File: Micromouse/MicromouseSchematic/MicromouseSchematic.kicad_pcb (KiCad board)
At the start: 2 copper layers, 0 parts

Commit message: Schematics clear, moved all footprints to pcb and voltage regulator completed. The layout begins
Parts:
- added C1: 0.47 μF, Capacitor_SMD:C_0201_0603Metric, F.Cu at (62.0, 97.2)
- added C11: 100nF, Capacitor_SMD:C_0402_1005Metric, F.Cu at (108.4, 161.7)
- added C19: 0.1u, Capacitor_SMD:C_0402_1005Metric, F.Cu at (251.6, 118.7)
- added C2: 22 µF, Capacitor_SMD:C_0402_1005Metric, F.Cu at (71.5, 38.0)
- added C20: 10p, Capacitor_SMD:C_0402_1005Metric, F.Cu at (251.6, 120.6)
- added C21: 10p, Capacitor_SMD:C_0402_1005Metric, F.Cu at (251.6, 122.6)
- added C22: 2.2u, Capacitor_SMD:C_0402_1005Metric, F.Cu at (251.6, 124.6)
- added C23: 2.2u, Capacitor_SMD:C_0402_1005Metric, F.Cu at (251.6, 126.5)
- added C24: 100n, Capacitor_SMD:C_0402_1005Metric, F.Cu at (251.6, 128.5)
- added C25: 100n, Capacitor_SMD:C_0402_1005Metric, F.Cu at (254.5, 118.7)
- added C26: 100n, Capacitor_SMD:C_0402_1005Metric, F.Cu at (254.5, 120.6)
- added C27: 100n, Capacitor_SMD:C_0402_1005Metric, F.Cu at (254.5, 122.6)
- added C28: 6.8p, Capacitor_SMD:C_0402_1005Metric, F.Cu at (254.5, 124.6)
- added C29: 100n, Capacitor_SMD:C_0402_1005Metric, F.Cu at (254.5, 126.5)
- added C3: 0.47 μF, Capacitor_SMD:C_0402_1005Metric, F.Cu at (59.3, 91.5)
- added C30: 100n, Capacitor_SMD:C_0402_1005Metric, F.Cu at (254.5, 128.5)
- added C31: 6.8p, Capacitor_SMD:C_0402_1005Metric, F.Cu at (257.4, 118.7)
- added C32: 10u, Capacitor_SMD:C_0402_1005Metric, F.Cu at (257.4, 120.6)
- added C33: 1u, Capacitor_SMD:C_0402_1005Metric, F.Cu at (257.4, 122.6)
- added C34: 10n, Capacitor_SMD:C_0402_1005Metric, F.Cu at (257.4, 124.6)
- added C35: 1u, Capacitor_SMD:C_0402_1005Metric, F.Cu at (257.4, 126.5)
- added C36: 0.47 μF, Capacitor_SMD:C_0402_1005Metric, F.Cu at (59.3, 93.4)
- added C37: 0.47 μF, Capacitor_SMD:C_0402_1005Metric, F.Cu at (59.3, 95.4)
- added C38: 0.1 μF, Capacitor_SMD:C_0402_1005Metric, F.Cu at (194.1, 37.0)
- added C39: 2.2 μF, Capacitor_SMD:C_0402_1005Metric, F.Cu at (194.1, 39.0)
- added C4: 220 nF, Capacitor_SMD:C_0402_1005Metric, F.Cu at (194.1, 29.2)
- added C40: 10 nF, Capacitor_SMD:C_0402_1005Metric, F.Cu at (194.1, 41.0)
- added C41: 1uF, Capacitor_SMD:C_0402_1005Metric, F.Cu at (129.5, 57.3)
- added C42: 1uF, Capacitor_SMD:C_0402_1005Metric, F.Cu at (129.5, 59.3)
- added C43: 1uF, Capacitor_SMD:C_0402_1005Metric, F.Cu at (129.5, 61.3)
- added C44: 1uF, Capacitor_SMD:C_0402_1005Metric, F.Cu at (129.5, 63.3)
- added C5: 100 nF, Capacitor_SMD:C_0402_1005Metric, F.Cu at (194.1, 31.1)
- added C6: 100 nF, Capacitor_SMD:C_0402_1005Metric, F.Cu at (194.1, 33.1)
- added C7: 10 μF, Capacitor_SMD:C_0402_1005Metric, F.Cu at (194.1, 35.1)
- added C9: 4.7uF, Capacitor_SMD:C_0402_1005Metric, F.Cu at (108.4, 159.7)
- added Cin_MD1: 22 μF, Capacitor_SMD:C_0402_1005Metric, F.Cu at (59.3, 97.4)
- added Cin_VR1: 10 µF, Capacitor_SMD:C_0402_1005Metric, F.Cu at (57.5, 38.0)
- added D1: SFH4550, LED_THT:LED_D5.0mm_IRGrey, F.Cu at (117.0, 31.0)
- added D2: SFH4550, LED_THT:LED_D5.0mm_IRGrey, F.Cu at (117.0, 38.4)
- added D3: SFH4550, LED_THT:LED_D5.0mm_IRGrey, F.Cu at (124.5, 31.0)
- added D4: SFH4550, LED_THT:LED_D5.0mm_IRGrey, F.Cu at (124.5, 38.4)
- added FB1: FerriteBead, Resistor_SMD:R_0805_2012Metric, F.Cu at (254.0, 141.5)
- added J1: Conn_01x06_MountingPin, Connector_JST:JST_PH_B6B-PH-K_1x06_P2.00mm_Vertical, F.Cu at (56.3, 80.1)
- added J10: Conn_01x06_MountingPin, Connector_JST:JST_ZH_B6B-ZR_1x06_P1.50mm_Vertical, F.Cu at (219.2, 156.6)
- added J2: Conn_01x06_MountingPin, Connector_JST:JST_PH_B6B-PH-K_1x06_P2.00mm_Vertical, F.Cu at (56.3, 86.7)
- added J3: Conn_01x03_Pin, Connector_JST:JST_PH_B3B-PH-K_1x03_P2.00mm_Vertical, F.Cu at (73.5, 41.5)
- added J4: Conn_01x02_Pin, Connector_JST:JST_PH_B2B-PH-K_1x02_P2.00mm_Vertical, F.Cu at (77.5, 35.5)
- added J5: Conn_01x06_MountingPin, Connector_JST:JST_ZH_B6B-ZR_1x06_P1.50mm_Vertical, F.Cu at (219.2, 151.1)
- added J6: IR_1, Connector_JST:JST_ZH_B4B-ZR_1x04_P1.50mm_Vertical, F.Cu at (117.0, 44.5)
- added J7: IR_2, Connector_JST:JST_ZH_B4B-ZR_1x04_P1.50mm_Vertical, F.Cu at (116.9, 50.1)
- added J8: IR_3, Connector_JST:JST_ZH_B4B-ZR_1x04_P1.50mm_Vertical, F.Cu at (117.0, 55.6)
- added J9: IR_4, Connector_JST:JST_ZH_B4B-ZR_1x04_P1.50mm_Vertical, F.Cu at (117.0, 61.1)
- added Q1: SFH300, LED_THT:LED_D5.0mm_Clear, F.Cu at (131.9, 31.0)
- added Q2: DMN3065LW-7, MM_DMN3065LW-7:DMN3065LW-7, F.Cu at (131.0, 43.9)
- added Q3: DMN3065LW-7, MM_DMN3065LW-7:DMN3065LW-7, F.Cu at (131.0, 47.5)
- added Q4: DMN3065LW-7, MM_DMN3065LW-7:DMN3065LW-7, F.Cu at (130.9, 51.2)
- added Q5: DMN3065LW-7, MM_DMN3065LW-7:DMN3065LW-7, F.Cu at (131.0, 54.6)
- added Q6: SFH300, LED_THT:LED_D5.0mm_Clear, F.Cu at (131.9, 38.4)
- added Q7: SFH300, LED_THT:LED_D5.0mm_Clear, F.Cu at (139.4, 31.0)
- added Q8: SFH300, LED_THT:LED_D5.0mm_Clear, F.Cu at (139.4, 38.4)
- added R1: 10k, Resistor_SMD:R_0603_1608Metric, F.Cu at (104.9, 153.1)
- added R2: 10k, Resistor_SMD:R_0603_1608Metric, F.Cu at (104.9, 155.6)
- added R20: 10k, Resistor_SMD:R_0603_1608Metric, F.Cu at (253.8, 144.3)
- added R21: 5 kΩ, Resistor_SMD:R_0805_2012Metric, F.Cu at (63.0, 92.0)
- added R22: 5 kΩ, Resistor_SMD:R_0805_2012Metric, F.Cu at (63.0, 94.9)
- added R23: 10 kΩ, Resistor_SMD:R_0603_1608Metric, F.Cu at (197.5, 29.4)
- added R24: 10 kΩ, Resistor_SMD:R_0603_1608Metric, F.Cu at (197.5, 31.9)
- added R25: 10k, Resistor_SMD:R_0603_1608Metric, F.Cu at (126.1, 43.4)
- added R26: 10 kΩ, Resistor_SMD:R_0603_1608Metric, F.Cu at (197.5, 34.5)
- added R27: 10 kΩ, Resistor_SMD:R_0603_1608Metric, F.Cu at (197.5, 37.0)
- added R28: 100, Resistor_SMD:R_0603_1608Metric, F.Cu at (126.1, 45.9)
- added R29: 10k, Resistor_SMD:R_0603_1608Metric, F.Cu at (126.1, 48.4)
- added R3: 10k, Resistor_SMD:R_0603_1608Metric, F.Cu at (104.9, 158.1)
- added R30: 100, Resistor_SMD:R_0603_1608Metric, F.Cu at (126.1, 50.9)
- added R31: 10k, Resistor_SMD:R_0603_1608Metric, F.Cu at (126.1, 53.5)
- added R32: 100, Resistor_SMD:R_0603_1608Metric, F.Cu at (126.1, 56.0)
- added R33: 10k, Resistor_SMD:R_0603_1608Metric, F.Cu at (126.1, 58.5)
- added R34: 100, Resistor_SMD:R_0603_1608Metric, F.Cu at (126.1, 61.0)
- added R35: 10 kΩ, Resistor_SMD:R_0603_1608Metric, F.Cu at (51.3, 78.6)
- added R36: 10 kΩ, Resistor_SMD:R_0603_1608Metric, F.Cu at (51.3, 81.1)
- added R37: 10 kΩ, Resistor_SMD:R_0603_1608Metric, F.Cu at (51.3, 83.7)
- added R38: 10 kΩ, Resistor_SMD:R_0603_1608Metric, F.Cu at (51.3, 86.2)
- added R39: 10 kΩ, Resistor_SMD:R_0603_1608Metric, F.Cu at (51.3, 88.7)
- added R4: 10k, Resistor_SMD:R_0603_1608Metric, F.Cu at (104.9, 160.6)
- added R40: 10 kΩ, Resistor_SMD:R_0603_1608Metric, F.Cu at (51.3, 91.2)
- added R41: 10 kΩ, Resistor_SMD:R_0603_1608Metric, F.Cu at (51.3, 93.7)
- added R42: 10 kΩ, Resistor_SMD:R_0603_1608Metric, F.Cu at (51.3, 96.2)
- added Renb1: 30kΩ, Resistor_SMD:R_0603_1608Metric, F.Cu at (60.7, 36.2)
- added Rent1: 62kΩ, Resistor_SMD:R_0603_1608Metric, F.Cu at (60.7, 39.6)
- added SW1: SW_Push, Button_Switch_THT:SW_SPST_Omron_B3F-40xx, F.Cu at (218.7, 122.9)
- added SW2: SW_Push, Button_Switch_THT:SW_SPST_Omron_B3F-40xx, F.Cu at (218.7, 138.5)
- added U1: VL53L1CXV0FY1, MM_VL53L4CDV0DH-1:LGA12_STM, F.Cu at (109.2, 155.3)
- added U11: MP6550GG-Z, MM_MP6550G-Z:MP6550_MNP, F.Cu at (55.5, 97.0)
- added U3: ICM-42688-P, MM_ICM_42688_P:ICM_42688_P, F.Cu at (202.2, 30.2)
- added U4: LIS2MDLTR, MM_LIS2MDLTR:LIS2MDLTR, F.Cu at (201.7, 34.1)
- added U5: STM32F746VETx, Package_QFP:LQFP-100_14x14mm_P0.5mm, F.Cu at (242.5, 146.0)
- added U7: MP6550GG-Z, MM_MP6550G-Z:MP6550_MNP, F.Cu at (55.5, 92.7)
- added VR1: TPSM861253RDXR, MM_TPSM861253RDXR:TPSM861253RDXR, F.Cu at (67.5, 38.3)
- added Y1: 8MHz, Crystal:Crystal_SMD_5032-2Pin_5.0x3.2mm, F.Cu at (253.9, 132.1)
- added Y2: 32.768kHz, Crystal:Crystal_SMD_3215-2Pin_3.2x1.5mm, F.Cu at (254.3, 138.4)
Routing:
- net GND: track 0.00 -> 44.0 mm
- net +7.4V: track 0.00 -> 31.5 mm
- net +3.3V: track 0.00 -> 16.8 mm
- net Net-(VR1-EN): track 0.00 -> 6.92 mm
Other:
- board outline added: 30.7 x 18.7 mm
- board text added: "Base board"
- board text added: "IMU&Mag"
- board text added: "IR Sensors"
- board text added: "Motor Drivers"
- board text added: "ToF"
- board text added: "Voltage regulator"

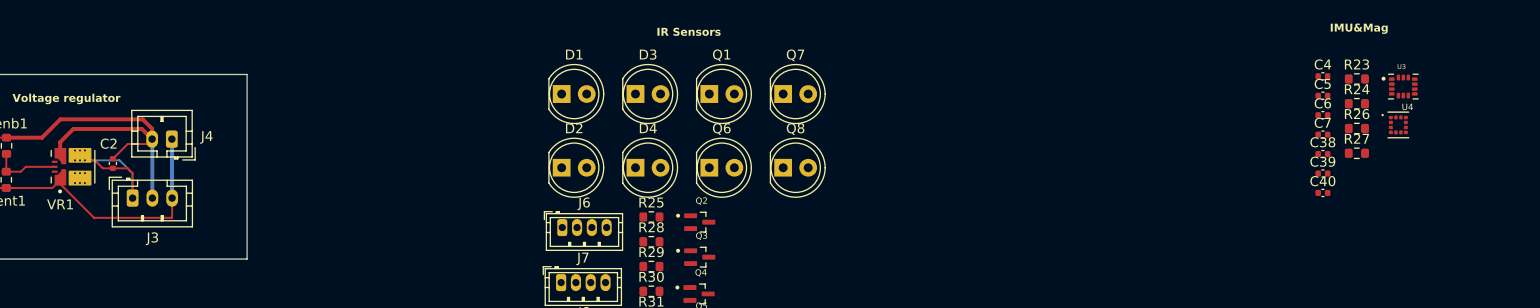
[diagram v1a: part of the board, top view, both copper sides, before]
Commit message: to-do IMU+Mag figure it out or mutli layer pcb?
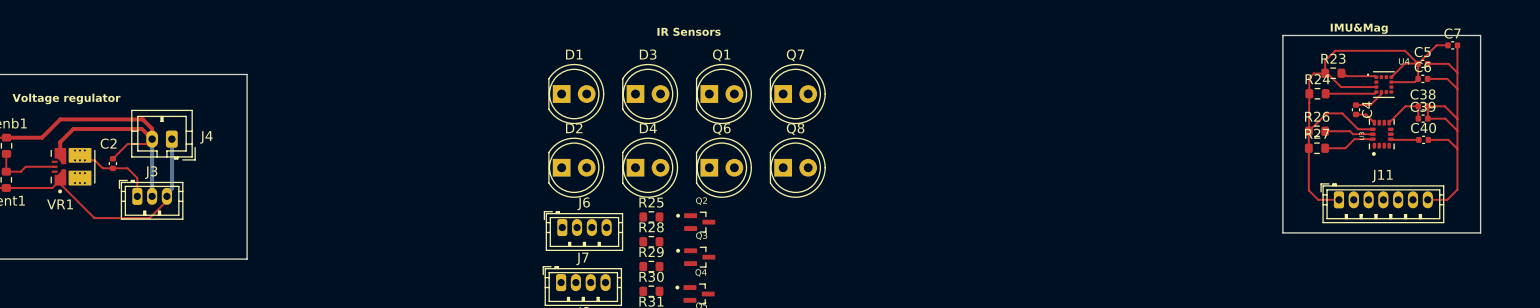
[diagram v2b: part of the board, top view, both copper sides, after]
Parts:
- added J11: Conn_01x07_Pin, Connector_JST:JST_ZH_B7B-ZR_1x07_P1.50mm_Vertical, F.Cu at (195.7, 41.7)
- J3: footprint Connector_JST:JST_PH_B3B-PH-K_1x03_P2.00mm_Vertical -> Connector_JST:JST_ZH_B3B-ZR_1x03_P1.50mm_Vertical
- moved C7 16.0 mm to (207.2, 26.0)
- moved C39 11.6 mm to (204.2, 33.5)
- moved C40 11.5 mm to (204.3, 35.6)
- moved C38 11.2 mm to (204.2, 32.2)
- moved C6 10.8 mm to (204.2, 29.4)
- moved C5 10.6 mm to (204.2, 27.9)
- moved U3 5.30 mm to (200.1, 35.0), turned to 90 degrees
- moved C4 4.77 mm to (197.4, 32.5), turned to -90 degrees
- moved U4 4.34 mm to (200.3, 30.0)
- moved R24 4.12 mm to (193.6, 30.9)
- moved R27 4.07 mm to (193.5, 36.5)
- moved R26 4.05 mm to (193.5, 34.7)
- moved R23 2.46 mm to (195.2, 28.9)
- moved J3 0.51 mm to (74.0, 41.3)
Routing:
- net +3.3V: track 16.8 -> 69.1 mm
- net GND: track 44.0 -> 82.5 mm
- net I2C_SDA: track 0.00 -> 10.5 mm
- net I2C_SCL: track 0.00 -> 8.65 mm
- net Net-(U4-C1): track 0.00 -> 3.24 mm
- net +7.4V: track 31.5 -> 30.3 mm
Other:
- board size 30.7 x 18.7 mm -> 155.7 x 22.6 mm

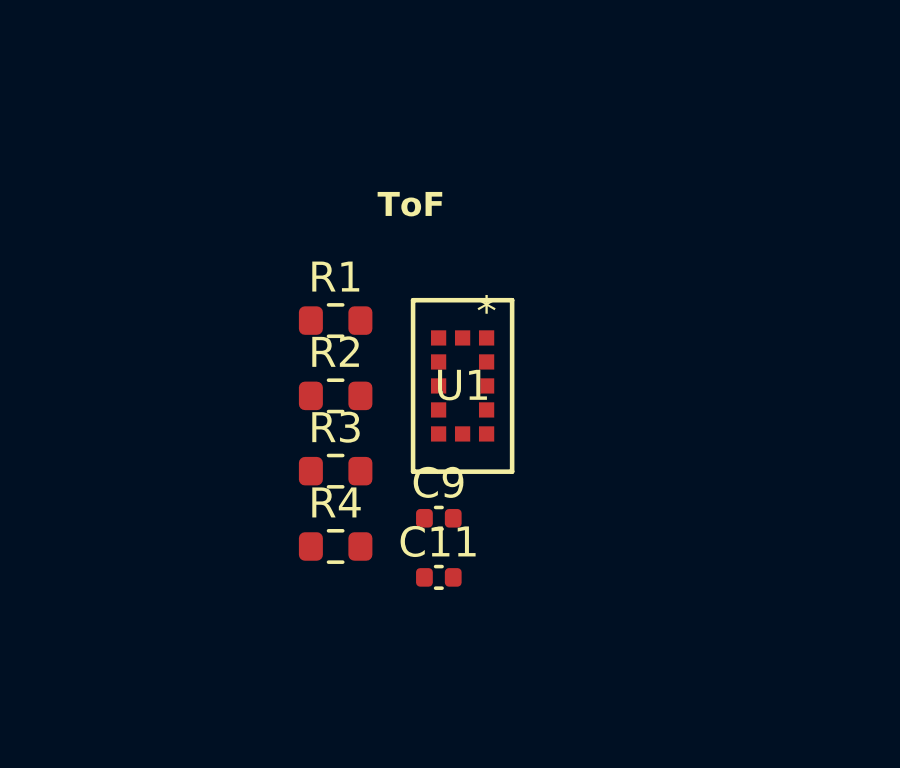
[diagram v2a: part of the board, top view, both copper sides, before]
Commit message: Add ToF sensor connector (J13) to schematic and did TOF PCB layout
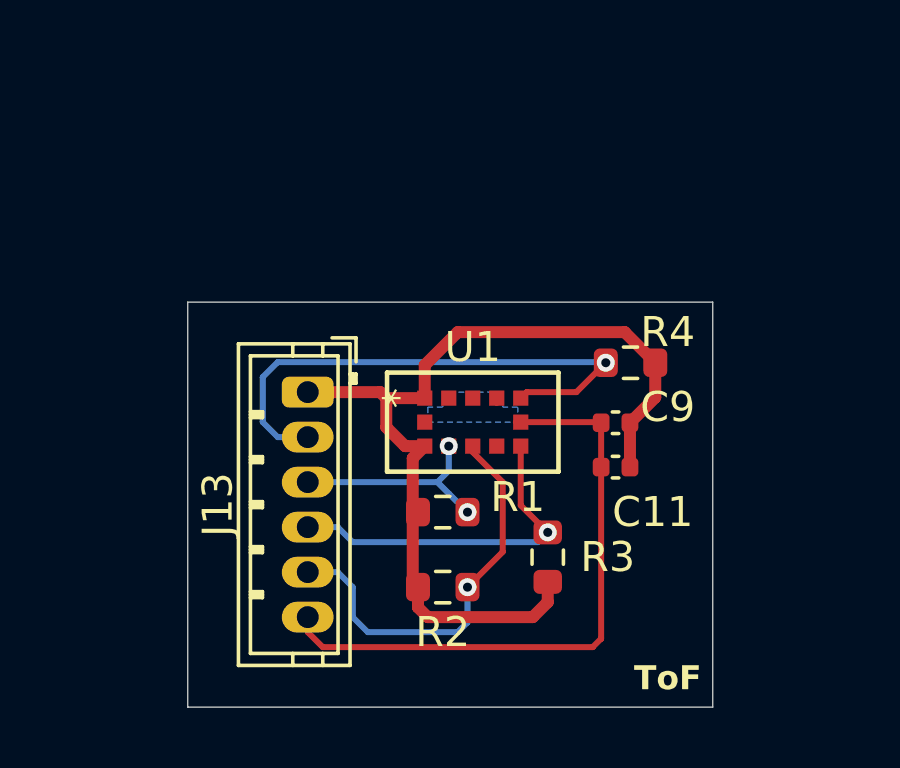
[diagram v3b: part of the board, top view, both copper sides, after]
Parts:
- added J13: Conn_01x06_Pin, Connector_JST:JST_ZH_B6B-ZR_1x06_P1.50mm_Vertical, F.Cu at (104.0, 155.5)
- moved R4 11.6 mm to (114.8, 154.5), turned to 180 degrees
- moved R3 7.63 mm to (112.0, 161.0), turned to 90 degrees
- moved R1 7.32 mm to (108.5, 159.5)
- moved R2 7.31 mm to (108.5, 162.0)
- moved C11 6.94 mm to (114.3, 158.0), turned to 180 degrees
- moved C9 6.70 mm to (114.3, 156.5), turned to 180 degrees
- moved U1 1.25 mm to (109.5, 156.5), turned to 90 degrees
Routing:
- net +3.3V: track 69.1 -> 100.2 mm
- net GND: track 82.5 -> 103.4 mm
- net TOF_CE: track 0.00 -> 18.2 mm, vias 0 -> 1
- net I2C_SDA: track 10.5 -> 24.1 mm, vias 0 -> 1
- net TOF_INT: track 0.00 -> 11.6 mm, vias 0 -> 1
- net I2C_SCL: track 8.65 -> 15.7 mm, vias 0 -> 2
- added copper zone on B.Cu, net GND
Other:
- board size 155.7 x 22.6 mm -> 155.7 x 141 mm
